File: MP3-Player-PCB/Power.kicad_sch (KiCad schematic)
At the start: 41 parts, among them J201 Conn_01x02_Socket, J202 USB_C_Receptacle_USB2.0_16P, U201 BQ24259, U202 USBLC6-2SC6, U203 TPS7A2033PDBVR, U204 TPS7A2033PDBVR

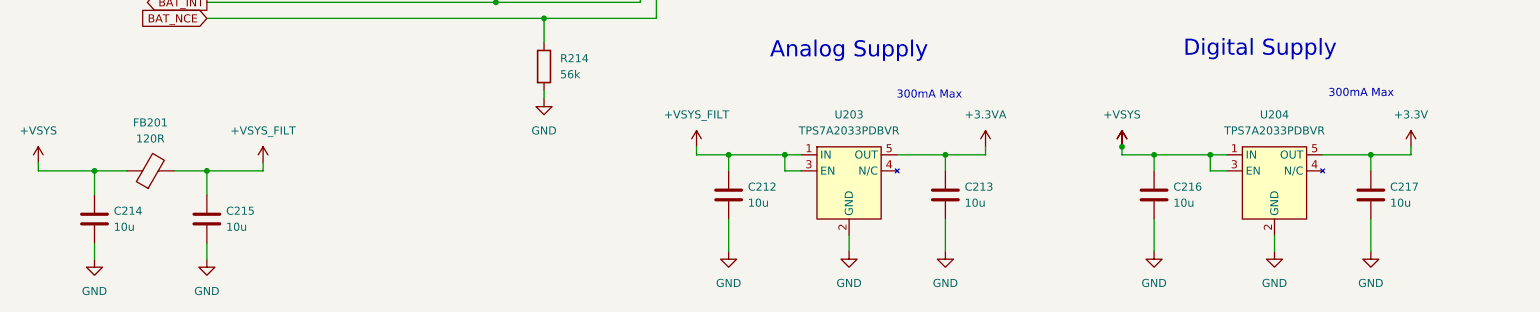
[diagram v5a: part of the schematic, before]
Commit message: Added esd protection to audiojack and sd card. Also added jack detection on audiojack
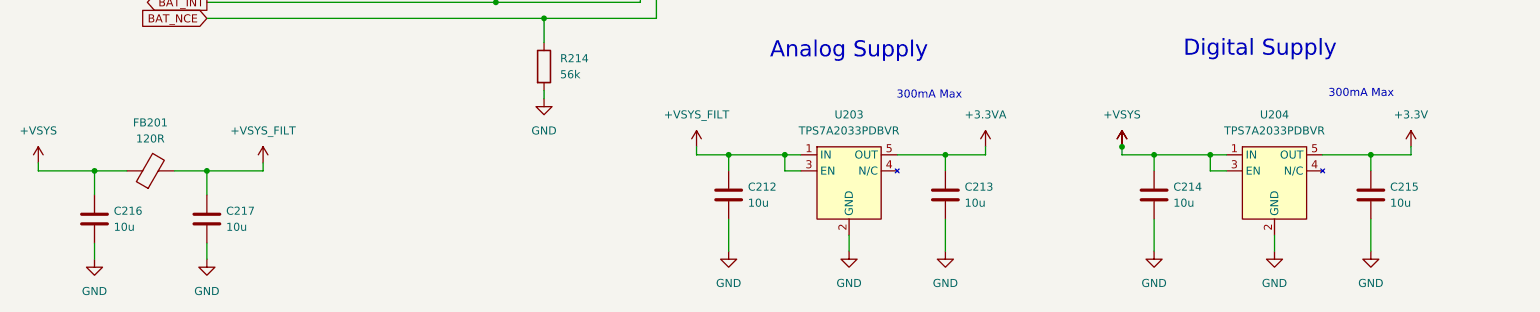
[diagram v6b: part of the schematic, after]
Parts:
- renumbered C216 to C214, C217 to C215, C214 to C216, C215 to C217
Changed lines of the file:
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@@
 		(dnp no)
 		(fields_autoplaced yes)
-		(property "Reference" "#PWR0234"
+		(property "Reference" "#PWR0233"
 			(at 224.79 147.32 0)
 			(effects
@@
 			(project "MP3-Player"
 				(path "/3f51ea9b-d2e1-4711-a47c-269e1b97e0f4/156723cf-95cb-4e74-b8dc-320a10f9d20f"
-					(reference "#PWR0234")
+					(reference "#PWR0233")
 					(unit 1)
 				)
@@
 		(dnp no)
 		(fields_autoplaced yes)
-		(property "Reference" "#PWR0236"
+		(property "Reference" "#PWR0224"
 			(at 200.66 128.27 0)
 			(effects
@@
 			(project "MP3-Player"
 				(path "/3f51ea9b-d2e1-4711-a47c-269e1b97e0f4/156723cf-95cb-4e74-b8dc-320a10f9d20f"
-					(reference "#PWR0236")
+					(reference "#PWR0224")
 					(unit 1)
 				)
@@
 		(on_board yes)
 		(dnp no)
-		(property "Reference" "C215"
+		(property "Reference" "C217"
 			(at 58.928 134.62 0)
 			(effects
@@
 			(project "MP3-Player"
 				(path "/3f51ea9b-d2e1-4711-a47c-269e1b97e0f4/156723cf-95cb-4e74-b8dc-320a10f9d20f"
-					(reference "C215")
+					(reference "C217")
 					(unit 1)
 				)
@@
 		(dnp no)
 		(fields_autoplaced yes)
-		(property "Reference" "#PWR0230"
+		(property "Reference" "#PWR0222"
 			(at 133.35 128.27 0)
 			(effects
@@
 			(project "MP3-Player"
 				(path "/3f51ea9b-d2e1-4711-a47c-269e1b97e0f4/156723cf-95cb-4e74-b8dc-320a10f9d20f"
-					(reference "#PWR0230")
+					(reference "#PWR0222")
 					(unit 1)
 				)
@@
 		(dnp no)
 		(fields_autoplaced yes)
-		(property "Reference" "#PWR0226"
+		(property "Reference" "#PWR0236"
 			(at 55.88 148.59 0)
 			(effects
@@
 			(project "MP3-Player"
 				(path "/3f51ea9b-d2e1-4711-a47c-269e1b97e0f4/156723cf-95cb-4e74-b8dc-320a10f9d20f"
-					(reference "#PWR0226")
+					(reference "#PWR0236")
 					(unit 1)
 				)
@@
 		(dnp no)
 		(fields_autoplaced yes)
-		(property "Reference" "#PWR0231"
+		(property "Reference" "#PWR0225"
 			(at 200.66 128.27 0)
 			(effects
@@
 			(project "MP3-Player"
 				(path "/3f51ea9b-d2e1-4711-a47c-269e1b97e0f4/156723cf-95cb-4e74-b8dc-320a10f9d20f"
-					(reference "#PWR0231")
+					(reference "#PWR0225")
 					(unit 1)
 				)
@@
 		(on_board yes)
 		(dnp no)
-		(property "Reference" "C216"
+		(property "Reference" "C214"
 			(at 208.788 130.81 0)
 			(effects
@@
 			(project "MP3-Player"
 				(path "/3f51ea9b-d2e1-4711-a47c-269e1b97e0f4/156723cf-95cb-4e74-b8dc-320a10f9d20f"
-					(reference "C216")
+					(reference "C214")
 					(unit 1)
 				)
@@
 		(on_board yes)
 		(dnp no)
-		(property "Reference" "C214"
+		(property "Reference" "C216"
 			(at 41.148 134.62 0)
 			(effects
@@
 			(project "MP3-Player"
 				(path "/3f51ea9b-d2e1-4711-a47c-269e1b97e0f4/156723cf-95cb-4e74-b8dc-320a10f9d20f"
-					(reference "C214")
+					(reference "C216")
 					(unit 1)
 				)
@@
 		(dnp no)
 		(fields_autoplaced yes)
-		(property "Reference" "#PWR0224"
+		(property "Reference" "#PWR0231"
 			(at 172.72 147.32 0)
 			(effects
@@
 			(project "MP3-Player"
 				(path "/3f51ea9b-d2e1-4711-a47c-269e1b97e0f4/156723cf-95cb-4e74-b8dc-320a10f9d20f"
-					(reference "#PWR0224")
+					(reference "#PWR0231")
 					(unit 1)
 				)
@@
 		(dnp no)
 		(fields_autoplaced yes)
-		(property "Reference" "#PWR0235"
+		(property "Reference" "#PWR0234"
 			(at 240.03 147.32 0)
 			(effects
@@
 			(project "MP3-Player"
 				(path "/3f51ea9b-d2e1-4711-a47c-269e1b97e0f4/156723cf-95cb-4e74-b8dc-320a10f9d20f"
-					(reference "#PWR0235")
+					(reference "#PWR0234")
 					(unit 1)
 				)
@@
 		(dnp no)
 		(fields_autoplaced yes)
-		(property "Reference" "#PWR0233"
+		(property "Reference" "#PWR0232"
 			(at 205.74 147.32 0)
 			(effects
@@
 			(project "MP3-Player"
 				(path "/3f51ea9b-d2e1-4711-a47c-269e1b97e0f4/156723cf-95cb-4e74-b8dc-320a10f9d20f"
-					(reference "#PWR0233")
+					(reference "#PWR0232")
 					(unit 1)
 				)
@@
 		(dnp no)
 		(fields_autoplaced yes)
-		(property "Reference" "#PWR0232"
+		(property "Reference" "#PWR0226"
 			(at 246.38 128.27 0)
 			(effects
@@
 			(project "MP3-Player"
 				(path "/3f51ea9b-d2e1-4711-a47c-269e1b97e0f4/156723cf-95cb-4e74-b8dc-320a10f9d20f"
-					(reference "#PWR0232")
+					(reference "#PWR0226")
 					(unit 1)
 				)
@@
 		(dnp no)
 		(fields_autoplaced yes)
-		(property "Reference" "#PWR0222"
+		(property "Reference" "#PWR0229"
 			(at 138.43 147.32 0)
 			(effects
@@
 			(project "MP3-Player"
 				(path "/3f51ea9b-d2e1-4711-a47c-269e1b97e0f4/156723cf-95cb-4e74-b8dc-320a10f9d20f"
-					(reference "#PWR0222")
+					(reference "#PWR0229")
 					(unit 1)
 				)
@@
 		(on_board yes)
 		(dnp no)
-		(property "Reference" "C217"
+		(property "Reference" "C215"
 			(at 243.078 130.81 0)
 			(effects
@@
 			(project "MP3-Player"
 				(path "/3f51ea9b-d2e1-4711-a47c-269e1b97e0f4/156723cf-95cb-4e74-b8dc-320a10f9d20f"
-					(reference "C217")
+					(reference "C215")
 					(unit 1)
 				)
@@
 		(dnp no)
 		(fields_autoplaced yes)
-		(property "Reference" "#PWR0229"
+		(property "Reference" "#PWR0223"
 			(at 179.07 128.27 0)
 			(effects
@@
 			(project "MP3-Player"
 				(path "/3f51ea9b-d2e1-4711-a47c-269e1b97e0f4/156723cf-95cb-4e74-b8dc-320a10f9d20f"
-					(reference "#PWR0229")
+					(reference "#PWR0223")
 					(unit 1)
 				)
@@
 		(dnp no)
 		(fields_autoplaced yes)
-		(property "Reference" "#PWR0225"
+		(property "Reference" "#PWR0235"
 			(at 38.1 148.59 0)
 			(effects
@@
 			(project "MP3-Player"
 				(path "/3f51ea9b-d2e1-4711-a47c-269e1b97e0f4/156723cf-95cb-4e74-b8dc-320a10f9d20f"
-					(reference "#PWR0225")
+					(reference "#PWR0235")
 					(unit 1)
 				)
@@
 		(dnp no)
 		(fields_autoplaced yes)
-		(property "Reference" "#PWR0223"
+		(property "Reference" "#PWR0230"
 			(at 157.48 147.32 0)
 			(effects
@@
 			(project "MP3-Player"
 				(path "/3f51ea9b-d2e1-4711-a47c-269e1b97e0f4/156723cf-95cb-4e74-b8dc-320a10f9d20f"
-					(reference "#PWR0223")
+					(reference "#PWR0230")
 					(unit 1)
 				)

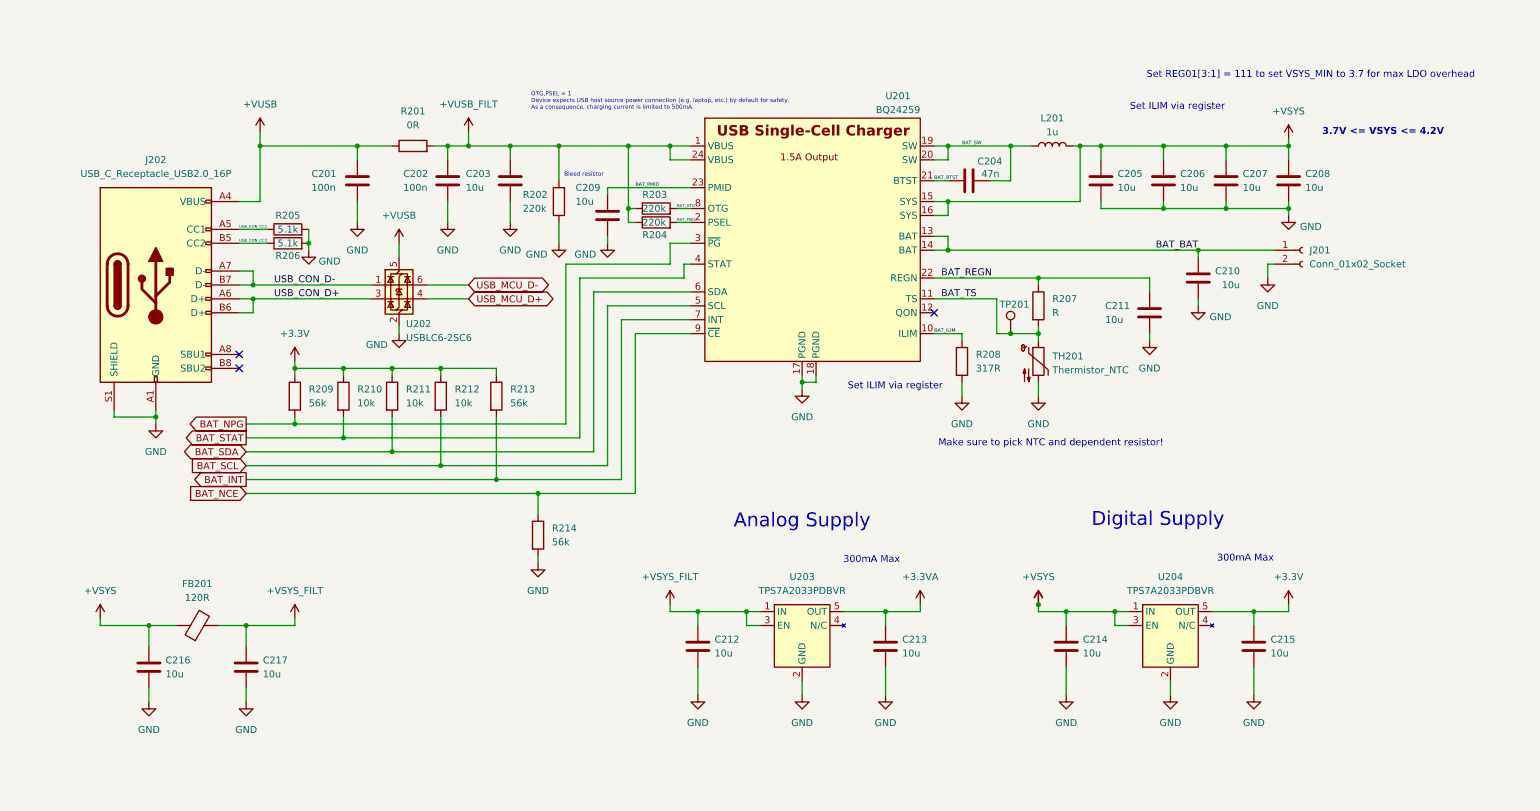
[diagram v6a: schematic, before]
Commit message: Added adc pin and voltage divider to read battery voltage. Also added charging status leds, and assigned some footprints
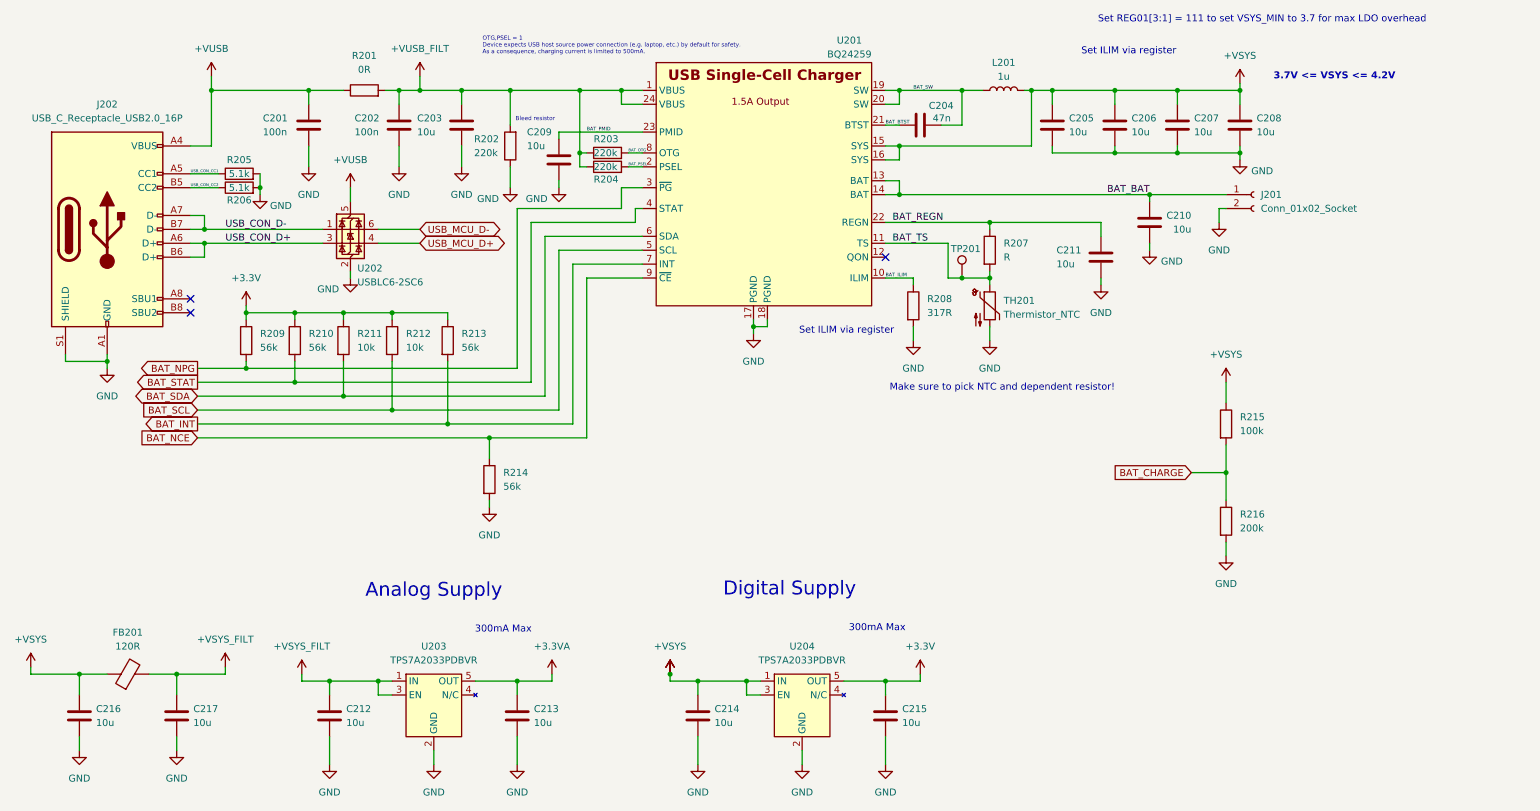
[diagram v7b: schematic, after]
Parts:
- added R215: 100k, symbol Device:R
- added R216: 200k, symbol Device:R
- C201, C202, C204: footprint (none) -> Capacitor_SMD:C_0603_1608Metric
- C203, C205, C206, C207, C208, C209, C210, C211, C212, C213, C214, C215, C216, C217: footprint (none) -> Capacitor_SMD:C_0805_2012Metric
- FB201: footprint (none) -> Inductor_SMD:L_0805_2012Metric
- J202: footprint (none) -> Connector_USB:USB_C_Receptacle_GCT_USB4105-xx-A_16P_TopMnt_Horizontal
- R210: value 10k -> 56k
- TP201: footprint (none) -> TestPoint:TestPoint_Pad_1.0x1.0mm
- U203, U204: footprint (none) -> Package_TO_SOT_SMD:SOT-23-5
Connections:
- net +VSYS: now also R215.1
- net GND: now also R216.2
- new net BAT_CHARGE: R215.2, R216.1
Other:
- moved on the sheet: C201, C202, C203, C204, C205, C206, C207, C208, C209, C210, C211, C212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

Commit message: Assigned all footprints
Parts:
- J201: footprint (none) -> Connector_JST:JST_EH_S2B-EH_1x02_P2.50mm_Horizontal
- L201: footprint (none) -> Inductor_SMD:L_Sunlord_SWPA3015S
- R201, TH201: footprint (none) -> Resistor_SMD:R_0603_1608Metric
- R202, R203, R204, R205, R206, R207, R208, R209, R210, R211, R212, R213, R214, R215, R216: footprint (none) -> Resistor_SMD:R_0402_1005Metric
- U201: footprint (none) -> Package_DFN_QFN:VQFN-24-1EP_4x4mm_P0.5mm_EP2.5x2.5mm
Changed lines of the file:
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@@
 			)
 		)
-		(property "Footprint" ""
+		(property "Footprint" "Resistor_SMD:R_0402_1005Metric"
 			(at 80.772 76.2 90)
 			(effects
@@
 			)
 		)
-		(property "Footprint" ""
+		(property "Footprint" "Resistor_SMD:R_0402_1005Metric"
 			(at 54.61 47.498 90)
 			(effects
@@
 			)
 		)
-		(property "Footprint" ""
+		(property "Footprint" "Connector_JST:JST_EH_S2B-EH_1x02_P2.50mm_Horizontal"
 			(at 240.03 49.53 0)
 			(effects
@@
 			)
 		)
-		(property "Footprint" ""
+		(property "Footprint" "Resistor_SMD:R_0402_1005Metric"
 			(at 233.172 109.22 90)
 			(effects
@@
 			)
 		)
-		(property "Footprint" ""
+		(property "Footprint" "Resistor_SMD:R_0603_1608Metric"
 			(at 77.47 32.258 90)
 			(effects
@@
 			)
 		)
-		(property "Footprint" ""
+		(property "Footprint" "Package_DFN_QFN:VQFN-24-1EP_4x4mm_P0.5mm_EP2.5x2.5mm"
 			(at 149.86 27.94 0)
 			(effects
@@
 			)
 		)
-		(property "Footprint" ""
+		(property "Footprint" "Resistor_SMD:R_0402_1005Metric"
 			(at 189.992 59.69 90)
 			(effects
@@
 			)
 		)
-		(property "Footprint" ""
+		(property "Footprint" "Resistor_SMD:R_0402_1005Metric"
 			(at 71.882 76.2 90)
 			(effects
@@
 			)
 		)
-		(property "Footprint" ""
+		(property "Footprint" "Resistor_SMD:R_0603_1608Metric"
 			(at 191.77 68.58 0)
 			(effects
@@
 			)
 		)
-		(property "Footprint" ""
+		(property "Footprint" "Resistor_SMD:R_0402_1005Metric"
 			(at 90.932 76.2 90)
 			(effects
@@
 			)
 		)
-		(property "Footprint" ""
+		(property "Footprint" "Inductor_SMD:L_Sunlord_SWPA3015S"
 			(at 194.31 30.48 0)
 			(effects
@@
 			)
 		)
-		(property "Footprint" ""
+		(property "Footprint" "Resistor_SMD:R_0402_1005Metric"
 			(at 54.102 76.2 90)
 			(effects
@@
 			)
 		)
-		(property "Footprint" ""
+		(property "Footprint" "Resistor_SMD:R_0402_1005Metric"
 			(at 105.918 40.64 90)
 			(effects
@@
 			)
 		)
-		(property "Footprint" ""
+		(property "Footprint" "Resistor_SMD:R_0402_1005Metric"
 			(at 121.92 46.228 90)
 			(effects
@@
 			)
 		)
-		(property "Footprint" ""
+		(property "Footprint" "Resistor_SMD:R_0402_1005Metric"
 			(at 176.022 69.85 90)
 			(effects
@@
 			)
 		)
-		(property "Footprint" ""
+		(property "Footprint" "Resistor_SMD:R_0402_1005Metric"
 			(at 54.61 50.038 90)
 			(effects
@@
 			)
 		)
-		(property "Footprint" ""
+		(property "Footprint" "Resistor_SMD:R_0402_1005Metric"
 			(at 121.92 43.688 90)
 			(effects
@@
 			)
 		)
-		(property "Footprint" ""
+		(property "Footprint" "Resistor_SMD:R_0402_1005Metric"
 			(at 98.552 101.6 90)
 			(effects
@@
 			)
 		)
-		(property "Footprint" ""
+		(property "Footprint" "Resistor_SMD:R_0402_1005Metric"
 			(at 62.992 76.2 90)
 			(effects
@@
 			)
 		)
-		(property "Footprint" ""
+		(property "Footprint" "Resistor_SMD:R_0402_1005Metric"
 			(at 233.172 91.44 90)
 			(effects
